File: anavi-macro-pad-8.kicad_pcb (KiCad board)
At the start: 2 copper layers, 135 x 47.1 mm, 50 parts, among them J1 USB_B_Micro, J2 Conn_01x04_Female, J3 Conn_01x03_Male, J4 Conn_01x03_Male, J5 AVR-ISP-6, Q1 Q_NPN_BEC, SW1 SW_DIP_x01, SW2 SW_DIP_x01, SW3 SW_DIP_x01, SW4 SW_DIP_x01, SW5 SW_DIP_x01, SW6 SW_DIP_x01, SW7 SW_DIP_x01, SW8 SW_DIP_x01, U1 ATmega32U4-AU, Y1 Crystal

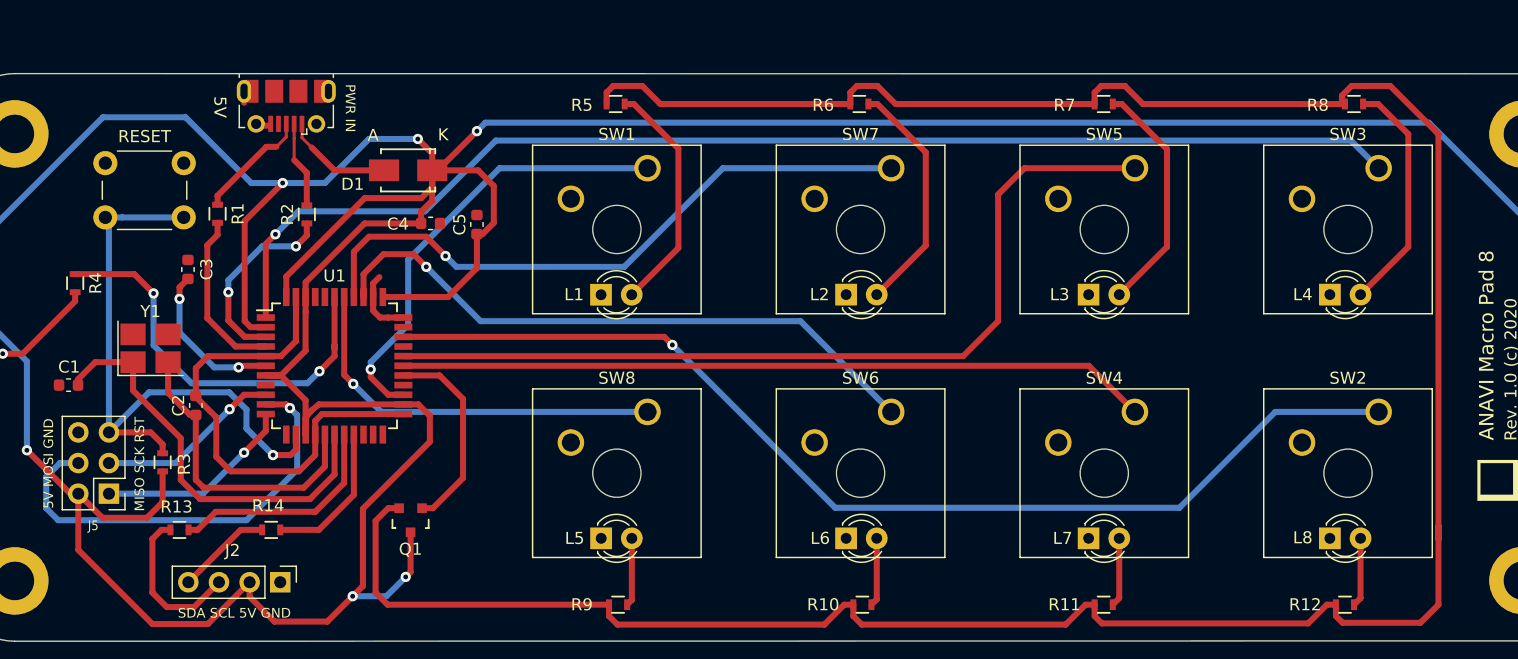
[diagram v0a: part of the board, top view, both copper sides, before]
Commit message: anavi-macro-pad-8.kicad_pcb: Update silkscreen
Update and improve labels on the front silkscreen.

Signed-off-by: Leon Anavi <leon@anavi.org>
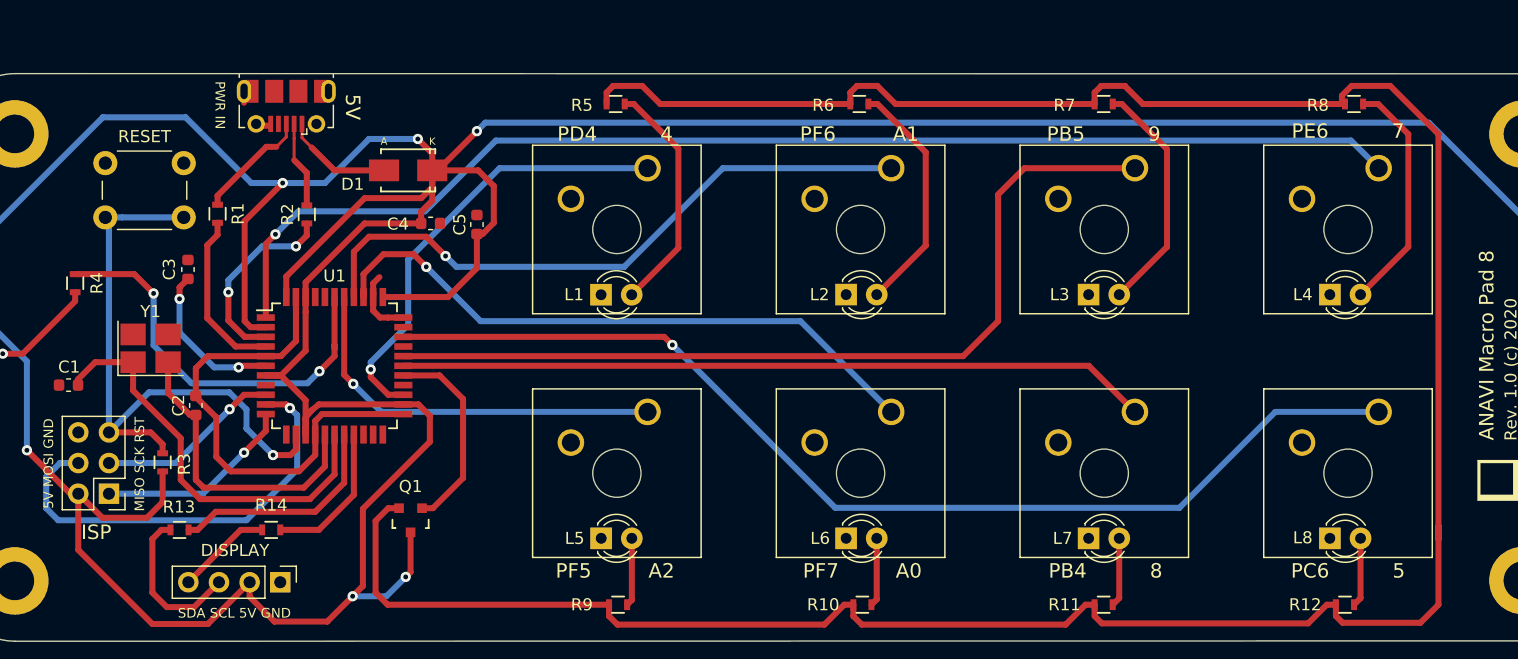
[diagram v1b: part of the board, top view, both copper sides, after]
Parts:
- Q1: value Q_NPN_BEC -> BC817 NPN
- Y1: value Crystal -> 16MHz
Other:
- board text added: "DISPLAY"
- board text added: "ISP"
- board text added: "PB4 8"
- board text added: "PB5 9"
- board text added: "PC6 5"
- board text added: "PD4 4"
- board text added: "PE6 7"
- board text added: "PF5 A2"
- board text added: "PF6 A1"
- board text added: "PF7 A0"

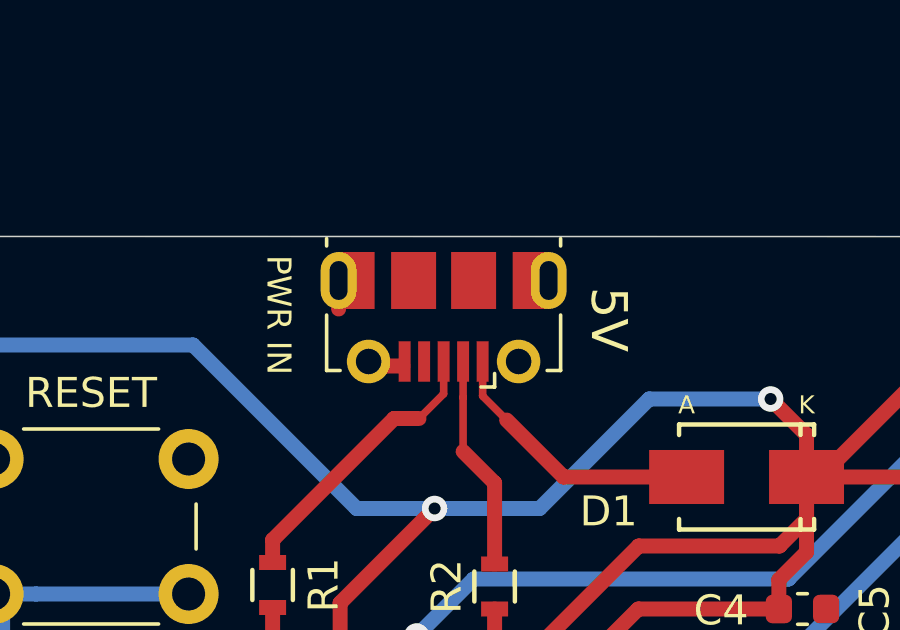
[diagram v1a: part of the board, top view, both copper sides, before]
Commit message: anavi-macro-pad-8.kicad_pcb: Update 5V labels
Rotate the labels near the microUSB to match the direction of
the other labels on the board.

Signed-off-by: Leon Anavi <leon@anavi.org>
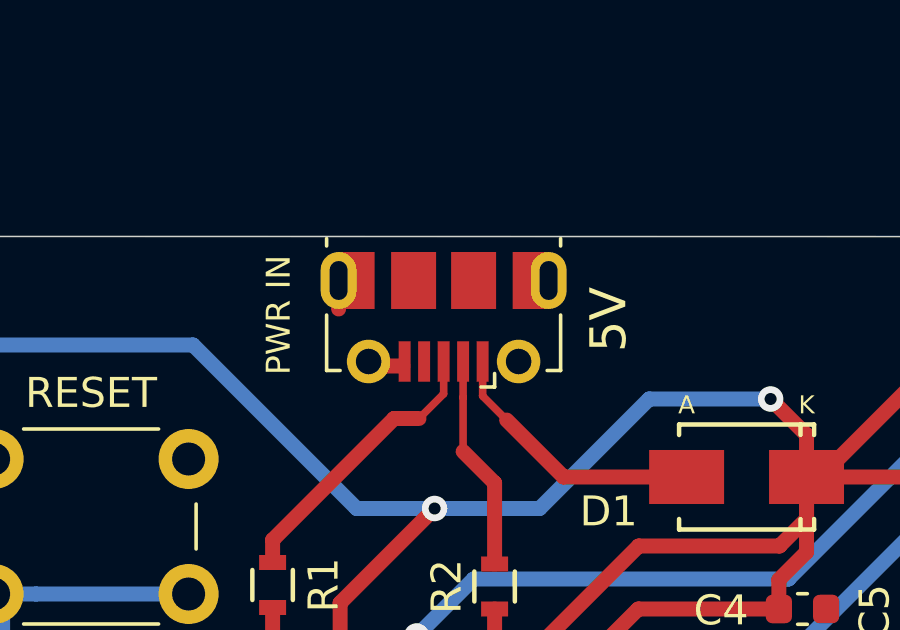
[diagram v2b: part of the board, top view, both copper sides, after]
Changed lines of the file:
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@@
     (effects (font (size 0.8 0.8) (thickness 0.1)))
   )
-  (gr_text 5V (at 78 57.75 270) (layer F.SilkS)
+  (gr_text 5V (at 78 57.75 90) (layer F.SilkS)
     (effects (font (size 1.2 1.2) (thickness 0.15)))
   )
-  (gr_text "PWR IN" (at 67 57.6 270) (layer F.SilkS)
+  (gr_text "PWR IN" (at 67 57.6 90) (layer F.SilkS)
     (effects (font (size 0.8 0.8) (thickness 0.1)))
   )

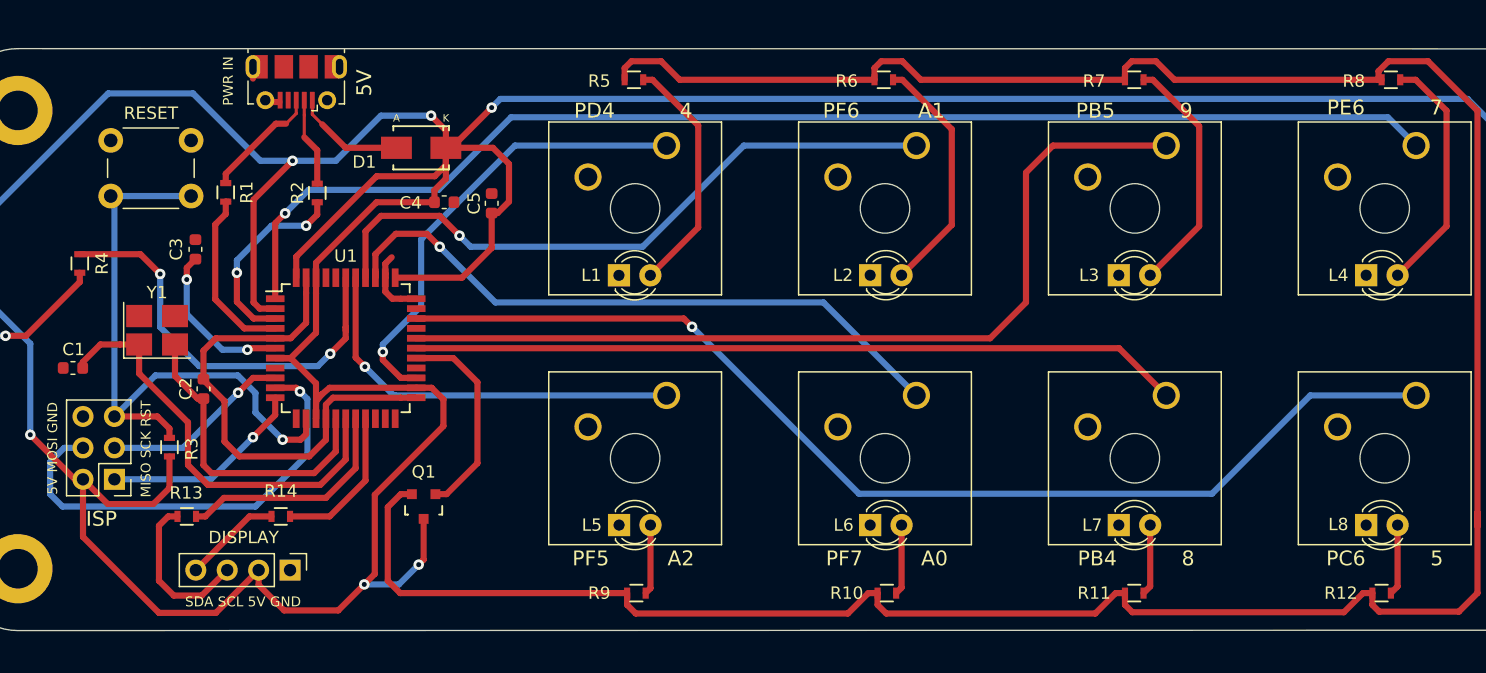
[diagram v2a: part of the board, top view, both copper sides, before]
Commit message: anavi-macro-pad-8.kicad_pcb: Change footprints
Replace footprints for all resistors and the transistor with
other same-sized footprints with bigger pads.

Signed-off-by: Leon Anavi <leon@anavi.org>
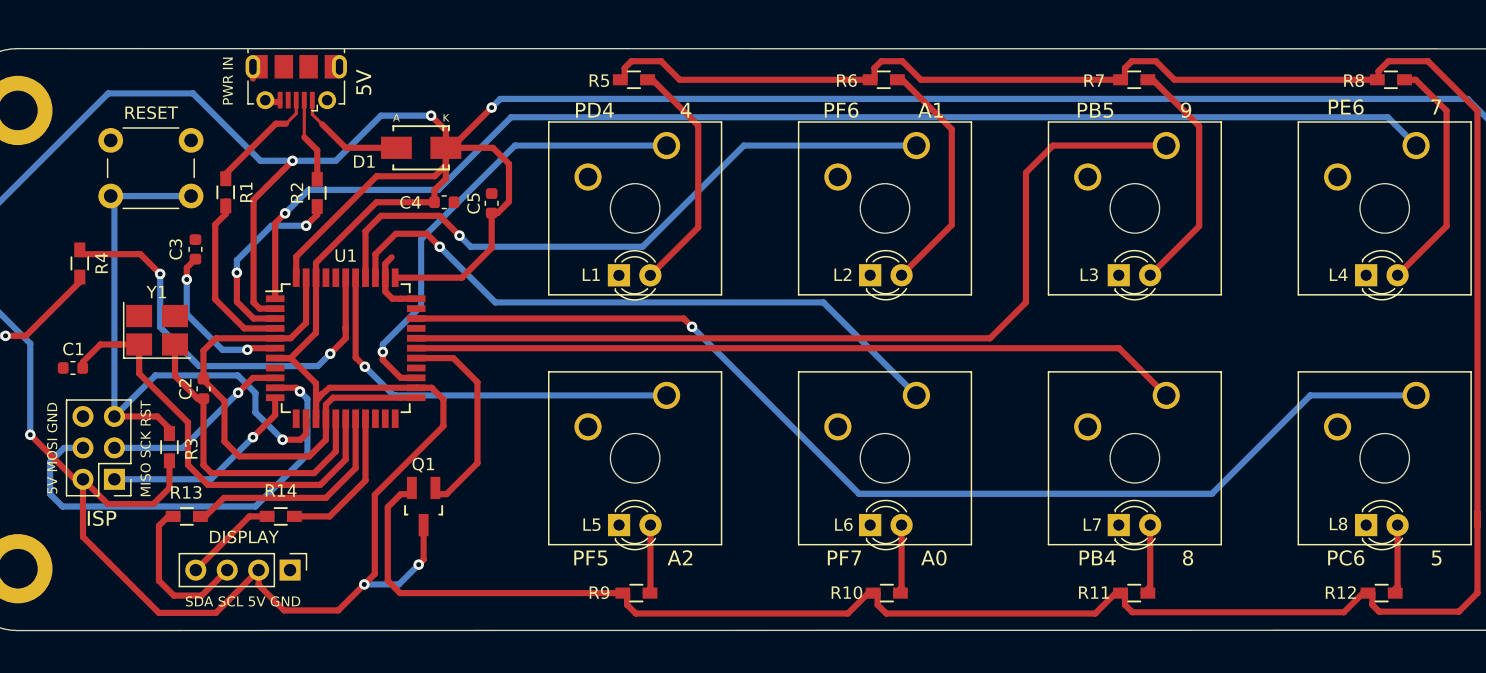
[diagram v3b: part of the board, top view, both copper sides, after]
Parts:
- Q1: footprint TO_SOT_Packages_SMD:SOT-23 -> TO_SOT_Packages_SMD:SOT-23_Handsoldering
- R1, R10, R11, R12, R13, R14, R2, R3, R4, R5, R6, R7, R8, R9: footprint Resistors_SMD:R_0603 -> Resistors_SMD:R_0603_HandSoldering

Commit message: anavi-macro-pad-8: Convert from KiCad 5 to 6
Convert the project from KiCad version 5 to version 6.

Signed-off-by: Leon Anavi <leon@anavi.org>
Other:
- net class Default removed
- net class usb removed
- net class vcc removed

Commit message: anavi-macro-pad-8: Fix I2C protection resistors
Resistors R13 and R14 had too large values. These are protection
resistors used in series on the SDA and SCL lines of the I2C. To
fix this issue the values of both resistors were set to 24 Ohms.

fixes #4

Reported-by: Heiko Lau <h.lau@ifam-erfurt.de>
Signed-off-by: Leon Anavi <leon@anavi.org>
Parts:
- R13, R14: value 4.7K -> 24R
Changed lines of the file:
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@@
       (effects (font (size 1 1) (thickness 0.15)))
     )
-    (fp_text value "4.7K" (at 3.05 -0.35) (layer "F.Fab")
+    (fp_text value "24R" (at 3.05 -0.35) (layer "F.Fab")
       (effects (font (size 1 1) (thickness 0.15)))
     )
@@
       (effects (font (size 1 1) (thickness 0.15)))
     )
-    (fp_text value "4.7K" (at 3.25 0) (layer "F.Fab")
+    (fp_text value "24R" (at 3.25 0) (layer "F.Fab")
       (effects (font (size 1 1) (thickness 0.15)))
     )
